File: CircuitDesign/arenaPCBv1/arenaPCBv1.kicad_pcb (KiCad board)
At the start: 2 copper layers, 13 parts, among them Q1 IRF520N

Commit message: PCB v1 finished
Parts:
- removed D2: LED, LED_THT:LED_D3.0mm
- removed U2: ~, Connector_PinHeader_1.27mm:PinHeader_1x03_P1.27mm_Vertical
- added C2: 100uF, Capacitor_THT:CP_Radial_D8.0mm_P3.50mm, F.Cu at (121.9, 104.2)
- added C3: 10uF, Capacitor_THT:CP_Radial_D5.0mm_P2.00mm, F.Cu at (152.3, 94.1)
- added C4: 100nF, Capacitor_THT:C_Disc_D3.8mm_W2.6mm_P2.50mm, F.Cu at (152.3, 76.2)
- added C5: 100nF, Capacitor_THT:C_Disc_D3.8mm_W2.6mm_P2.50mm, F.Cu at (152.3, 80.3)
- added C6: 10uF, Capacitor_THT:CP_Radial_D5.0mm_P2.00mm, F.Cu at (152.3, 100.7)
- added J1: ~, Connector_TE-Connectivity:TE_826576-2_1x02_P3.96mm_Vertical, F.Cu at (131.1, 103.6)
- added J2: ~, Connector_JST:JST_PH_B4B-PH-K_1x04_P2.00mm_Vertical, F.Cu at (109.7, 86.5)
- added J3: ~, Connector_JST:JST_PH_B2B-PH-K_1x02_P2.00mm_Vertical, F.Cu at (152.9, 106.7)
- added J4: ~, Connector_JST:JST_PH_B4B-PH-K_1x04_P2.00mm_Vertical, F.Cu at (109.7, 93.1)
- added J5: ~, Connector_PinSocket_2.00mm:PinSocket_1x02_P2.00mm_Vertical, F.Cu at (135.2, 93.6)
- added R2: 4k7, Resistor_THT:R_Axial_DIN0207_L6.3mm_D2.5mm_P15.24mm_Horizontal, F.Cu at (141.9, 68.0)
- added R3: 4k7, Resistor_THT:R_Axial_DIN0207_L6.3mm_D2.5mm_P15.24mm_Horizontal, F.Cu at (141.9, 72.1)
- C1: value C -> 220uF; footprint Capacitor_THT:CP_Radial_D13.0mm_P2.50mm -> Capacitor_THT:CP_Radial_D10.0mm_P5.00mm
- D1: value D -> 1N400X
- R1: value R -> 1k1; footprint Resistor_THT:R_Axial_DIN0207_L6.3mm_D2.5mm_P10.16mm_Horizontal -> Resistor_THT:R_Axial_DIN0207_L6.3mm_D2.5mm_P15.24mm_Horizontal
- U3: footprint Connector:JWT_A3963_1x02_P3.96mm_Vertical -> TerminalBlock_Phoenix:TerminalBlock_Phoenix_PT-1,5-2-3.5-H_1x02_P3.50mm_Horizontal
- U5: footprint Connector_PinHeader_1.27mm:PinHeader_1x06_P1.27mm_Vertical -> Connector_JST:JST_XH_B6B-XH-A_1x06_P2.50mm_Vertical
- U6: footprint 1_Bachelors_Footprints:2x7_test -> Connector_JST:JST_PHD_B16B-PHDSS_2x08_P2.00mm_Vertical
- U7: footprint Connector_PinHeader_1.27mm:PinHeader_1x04_P1.27mm_Vertical -> Connector_JST:JST_XH_B4B-XH-A_1x04_P2.50mm_Vertical
- moved U7 44.3 mm to (122.2, 95.0)
- moved D1 44.2 mm to (108.3, 108.3)
- moved R1 43.1 mm to (141.9, 64.0)
- moved U3 38.8 mm to (109.5, 101.0)
- moved U5 19.6 mm to (122.2, 87.2)
- moved Q1 18.4 mm to (141.4, 106.3)
- moved C1 17.4 mm to (141.7, 96.6)
- moved F1 14.8 mm to (143.0, 75.8)
- moved U1 11.9 mm to (108.8, 64.0)
- moved U4 11.9 mm to (125.6, 64.0)
- moved U6 11.1 mm to (141.6, 86.3)
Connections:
- C1 pad 1: S -> +12V
- C1 pad 2: D -> GND
- D1 pad 1: S -> +12V
- D1 pad 2: D -> GND
- F1 pad 2: S -> +12V
- Q1 pad 1: G -> /G
- Q1 pad 2: D -> /D
- Q1 pad 3: S -> +12V
- R1 pad 1: S -> +12V
- U1 pad 1: D -> GND
- U1 pad 15: S -> GND
- U1 pad 16: S -> +12V
- U1 pad 5: VMCU -> +3.3V
- U1 pad 6: VMCU -> +3.3V
- U1 pad 9: GND_MCU -> GND
- U3 pad 2: D -> GND
- U4 pad 1: D -> GND
- U4 pad 13: VMCU -> +3.3V
- U4 pad 2: VMCU -> +3.3V
- U4 pad 7: S -> +12V
- U4 pad 8: D -> GND
- U4 pad 9: D -> GND
- U5 pad 2: D -> GND
- U5 pad 3: Net-(U5-RST) -> Net-(U5-Pin_3)
- U5 pad 4: Net-(U5-GPIO0) -> Net-(U5-Pin_4)
- U5 pad 5: VMCU -> +3.3V
- U6 pad 1: VMCU -> GND
- U6 pad 10: Net-(U4-AIN2) -> Net-(U4-AIN1)
- U6 pad 11: Net-(U5-GPIO0) -> Net-(U5-Pin_3)
- U6 pad 12: Net-(U5-RST) -> Net-(U5-Pin_4)
- U6 pad 13: Net-(U2-SIGNAL) -> /G
- U6 pad 14: G -> Net-(J3-COM)
- U6 pad 2: GND_MCU -> +3.3V
- U6 pad 3: Net-(U1-STEP) -> Net-(U1-DIR)
- U6 pad 4: Net-(U1-DIR) -> Net-(U1-STEP)
- U6 pad 5: Net-(U1-MS3) -> Net-(U1-MS2)
- U6 pad 6: Net-(U1-MS2) -> Net-(U1-MS3)
- U6 pad 7: Net-(U1-MS1) -> Net-(U4-PWMA)
- U6 pad 8: Net-(U4-PWMA) -> Net-(U1-MS1)
- U6 pad 9: Net-(U4-AIN1) -> Net-(U4-AIN2)

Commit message: Before redoing PCB
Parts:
- removed U3: ~, TerminalBlock_Phoenix:TerminalBlock_Phoenix_PT-1,5-2-3.5-H_1x02_P3.50mm_Horizontal
- removed U4: ~, Module:Pololu_Breakout-16_15.2x20.3mm
- removed U5: ~, Connector_JST:JST_XH_B6B-XH-A_1x06_P2.50mm_Vertical
- removed U6: ~, Connector_JST:JST_PHD_B16B-PHDSS_2x08_P2.00mm_Vertical
- removed U7: ~, Connector_JST:JST_XH_B4B-XH-A_1x04_P2.50mm_Vertical
- added D2: STTH15RQ06, Package_TO_SOT_SMD:TO-263-2, F.Cu at (218.6, 61.2)
- added J6: ~, 2_Bachelors_footprints:LP127, F.Cu at (127.0, 99.1)
- added J7: ~, 2_Bachelors_footprints:CONN_B4P-VH_JST, F.Cu at (195.6, 61.0)
- added J8: ~, 2_Bachelors_footprints:CONN_B6B_VH_JST, F.Cu at (196.4, 87.1)
- added J9: ~, Connector_JST:JST_PHD_B16B-PHDSS_2x08_P2.00mm_Vertical, F.Cu at (149.9, 69.0)
- added R4: 330R, Resistor_SMD:R_1210_3225Metric_Pad1.30x2.65mm_HandSolder, F.Cu at (210.8, 69.5)
- added U2: ~, Module:Pololu_Breakout-16_15.2x20.3mm, F.Cu at (167.6, 90.2)
- C2: footprint Capacitor_THT:CP_Radial_D8.0mm_P3.50mm -> Capacitor_SMD:CP_Elec_10x10.5
- C3, C6: footprint Capacitor_THT:CP_Radial_D5.0mm_P2.00mm -> Capacitor_SMD:CP_Elec_6.3x4.5
- C4, C5: footprint Capacitor_THT:C_Disc_D3.8mm_W2.6mm_P2.50mm -> Capacitor_SMD:C_1210_3225Metric_Pad1.33x2.70mm_HandSolder
- D1: value 1N400X -> STTH15RQ06; footprint Diode_THT:D_DO-35_SOD27_P7.62mm_Horizontal -> Package_TO_SOT_SMD:TO-263-2
- F1: value RXEF300 -> MF-RG650-0; footprint Fuse:Fuse_Bourns_MF-RHT300 -> Fuse:Fuse_Bourns_MF-RG650
- J1: footprint Connector_TE-Connectivity:TE_826576-2_1x02_P3.96mm_Vertical -> 2_Bachelors_footprints:conn2_1-1123723-2_TEC
- J2, J4: footprint Connector_JST:JST_PH_B4B-PH-K_1x04_P2.00mm_Vertical -> 2_Bachelors_footprints:CONN_B4B-ZRLFSN_JST
- J3: footprint Connector_JST:JST_PH_B2B-PH-K_1x02_P2.00mm_Vertical -> 2_Bachelors_footprints:CONN_B2B-ZRLFSN_JST
- J5: footprint Connector_PinSocket_2.00mm:PinSocket_1x02_P2.00mm_Vertical -> Connector_PinSocket_2.54mm:PinSocket_1x02_P2.54mm_Vertical
- Q1: value IRF520N -> IRLB3034; footprint Package_TO_SOT_THT:TO-220-3_Vertical -> 2_Bachelors_footprints:IRF520N
- R1: value 1k1 -> 3K3; footprint Resistor_THT:R_Axial_DIN0207_L6.3mm_D2.5mm_P15.24mm_Horizontal -> Resistor_SMD:R_2512_6332Metric_Pad1.40x3.35mm_HandSolder
- R2, R3: value 4k7 -> 2K2; footprint Resistor_THT:R_Axial_DIN0207_L6.3mm_D2.5mm_P15.24mm_Horizontal -> Resistor_SMD:R_1210_3225Metric_Pad1.30x2.65mm_HandSolder
- moved C2 68.2 mm to (168.0, 53.8)
- moved U1 59.4 mm to (167.6, 72.4), turned to 90 degrees
- moved J3 52.1 mm to (160.0, 55.1), turned to -90 degrees
- moved C4 39.8 mm to (182.9, 101.6)
- moved D1 33.9 mm to (141.0, 99.1)
- moved J4 33.5 mm to (127.3, 64.5)
- moved J2 33.1 mm to (127.3, 58.4)
- moved C3 31.2 mm to (183.4, 96.5)
- moved J1 29.2 mm to (160.0, 99.1)
- moved C5 27.8 mm to (170.1, 101.6), turned to 180 degrees
- moved Q1 23.7 mm to (157.5, 88.9), turned to 180 degrees
- moved C6 18.3 mm to (170.2, 96.5), turned to 180 degrees
- moved R1 17.4 mm to (129.5, 76.2), turned to -90 degrees
- moved F1 17.2 mm to (135.9, 91.4), turned to 90 degrees
- moved C1 10.2 mm to (142.3, 86.4)
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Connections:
- D1 pad 1: +12V -> (no net)
- D1 pad 2: GND -> +12V
- J1 pad 1: /D -> +12V
- J1 pad 2: GND -> /D
- J2 pad 2: /SDA -> /SCL
- J2 pad 3: /SCL -> /SDA
- J4 pad 2: /SDA -> /SCL
- J4 pad 3: /SCL -> /SDA
- Q1 pad 3: +12V -> GND
- R2 pad 2: /SDA -> /SCL
- R3 pad 2: /SCL -> /SDA
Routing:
- net (no net): track 0.00 -> 404.0 mm, vias 0 -> 1
- net GND: track 0.00 -> 310.4 mm
- net +12V: track 0.00 -> 156.9 mm, vias 0 -> 1
- net +3.3V: track 0.00 -> 136.6 mm, vias 0 -> 1
- net /G: track 0.00 -> 39.5 mm
- net /SCL: track 0.00 -> 35.1 mm
- net Net-(J8-Pin_6): track 0.00 -> 31.3 mm
- net /SDA: track 0.00 -> 30.7 mm
- net Net-(J8-Pin_1): track 0.00 -> 28.2 mm
- net Net-(J7-Pin_1): track 0.00 -> 26.8 mm
- net Net-(J7-Pin_2): track 0.00 -> 25.2 mm
- net Net-(J7-Pin_3): track 0.00 -> 23.4 mm
- net Net-(J7-Pin_4): track 0.00 -> 21.7 mm
- net /D: track 0.00 -> 10.4 mm
- net Net-(J3-COM): track 0.00 -> 9.23 mm
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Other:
- board outline added: 96 x 69.6 mm

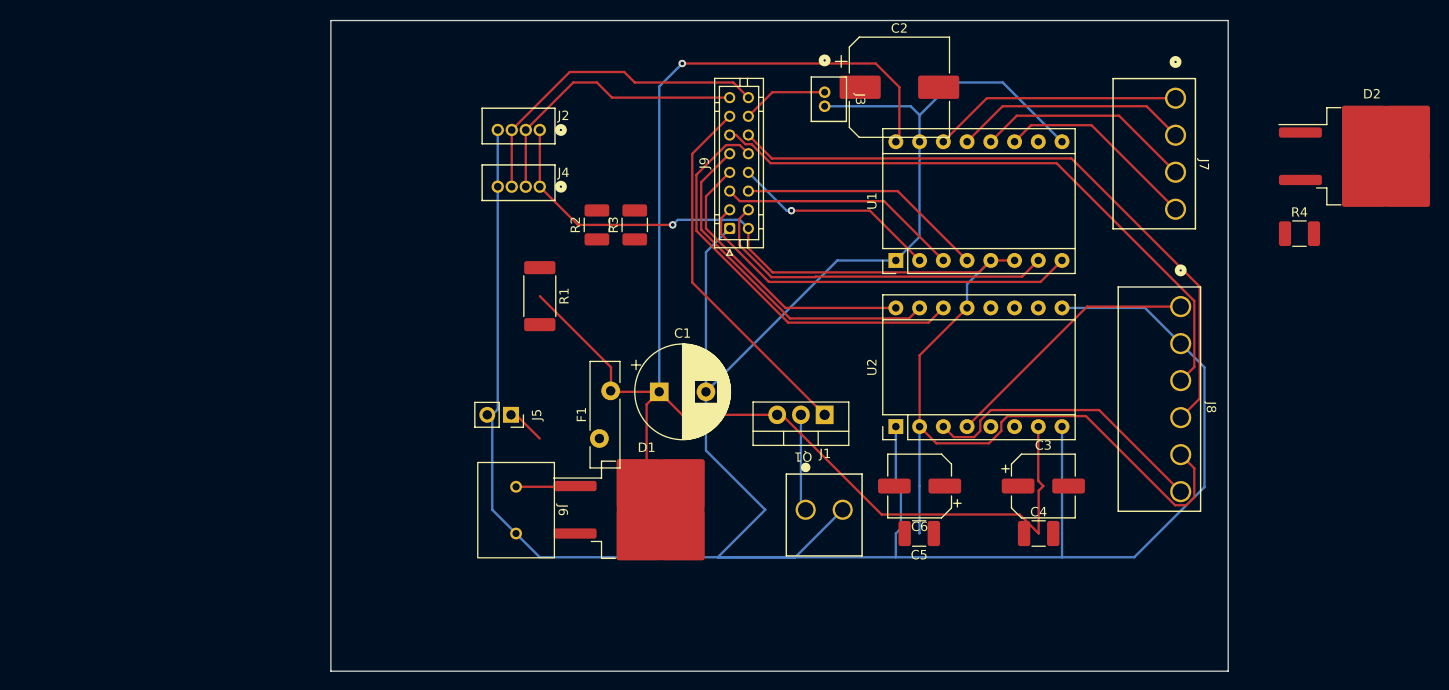
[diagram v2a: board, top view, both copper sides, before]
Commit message: PCB v2 finished, diode needs changing
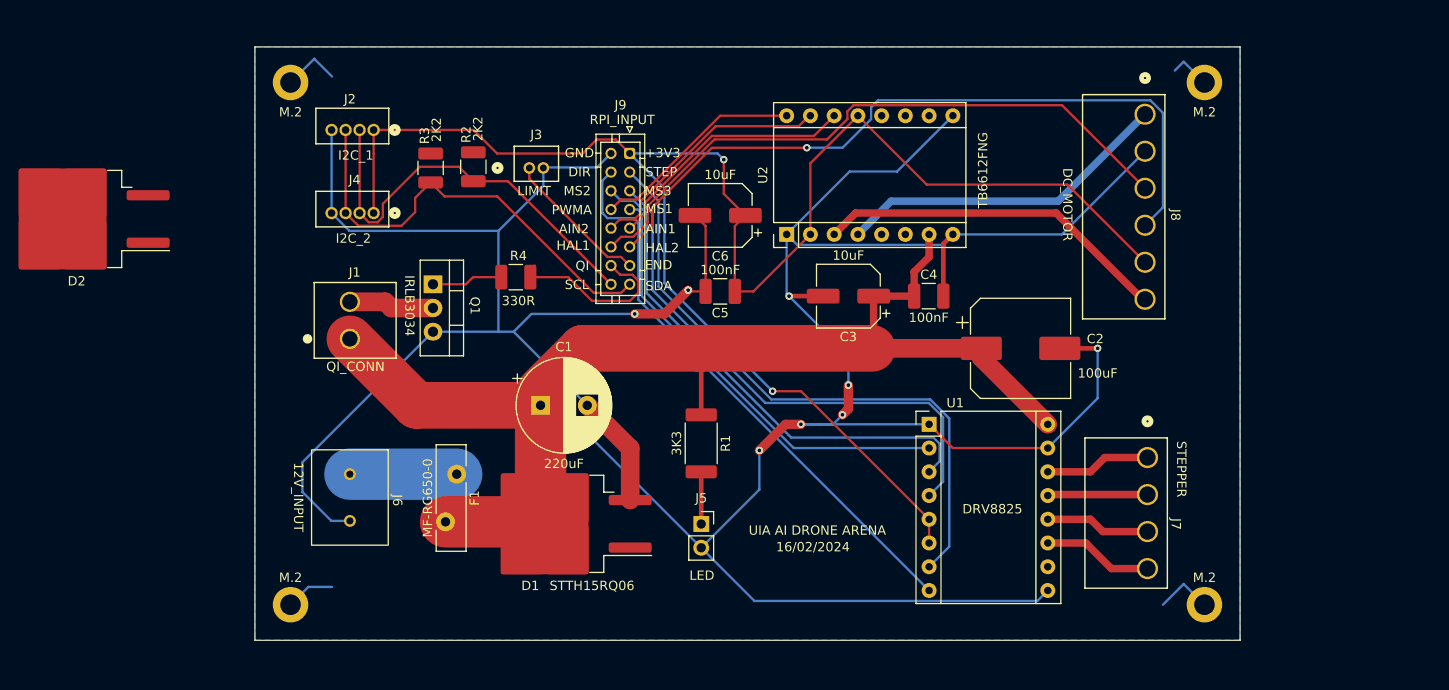
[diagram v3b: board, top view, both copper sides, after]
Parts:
- added M.2: MountingHole_2.2mm_M2_DIN965_Pad, MountingHole:MountingHole_2.2mm_M2_DIN965_Pad, F.Cu at (102.9, 53.3)
- added M.2: MountingHole_2.2mm_M2_DIN965_Pad, MountingHole:MountingHole_2.2mm_M2_DIN965_Pad, F.Cu at (200.7, 109.2)
- added M.2: MountingHole_2.2mm_M2_DIN965_Pad, MountingHole:MountingHole_2.2mm_M2_DIN965_Pad, F.Cu at (102.9, 109.2)
- added M.2: MountingHole_2.2mm_M2_DIN965_Pad, MountingHole:MountingHole_2.2mm_M2_DIN965_Pad, F.Cu at (200.7, 53.3)
- moved D2 138.8 mm to (80.0, 67.9), turned to 180 degrees
- moved R4 84.0 mm to (127.0, 74.2), turned to 180 degrees
- moved J1 54.7 mm to (109.2, 78.7), turned to 90 degrees
- moved Q1 41.0 mm to (118.1, 77.5), turned to -90 degrees
- moved J7 38.6 mm to (192.6, 99.4)
- moved C6 36.0 mm to (148.8, 67.6)
- moved C5 33.5 mm to (148.8, 75.7)
- moved J3 31.8 mm to (129.1, 62.5), turned to 0 degrees
- moved C2 30.8 mm to (181.0, 81.8)
- moved C3 29.1 mm to (162.6, 76.2), turned to 180 degrees
- moved C4 28.0 mm to (171.2, 76.2)
- moved U2 23.7 mm to (156.0, 69.6)
- moved J5 23.5 mm to (146.8, 100.6), turned to 0 degrees
- moved R1 23.4 mm to (146.8, 92.0)
- moved R3 22.7 mm to (117.9, 62.5), turned to -90 degrees
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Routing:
- net (no net): track 404.0 -> 0.00 mm, vias 1 -> 0
- net GND: track 310.4 -> 396.4 mm, vias 0 -> 8
- net Net-(J8-Pin_4): track 0.00 -> 78.8 mm, vias 0 -> 1
- net Net-(J8-Pin_3): track 0.00 -> 68.6 mm
- net Net-(J9-STEP): track 0.00 -> 67.2 mm
- net Net-(J9-DIR): track 0.00 -> 61.3 mm
- net Net-(J9-MS3): track 0.00 -> 57.4 mm
- net Net-(J9-MS2): track 0.00 -> 54.8 mm
- net Net-(J9-MS1): track 0.00 -> 47.8 mm
- net +3.3V: track 136.6 -> 183.8 mm, vias 1 -> 2
- net /G: track 39.5 -> 7.63 mm
- net Net-(J9-AIN1): track 0.00 -> 27.5 mm
- net Net-(J9-AIN2): track 0.00 -> 27.1 mm
- net +12V: track 156.9 -> 130.0 mm, vias 1 -> 0
- net Net-(J9-PWMA): track 0.00 -> 23.0 mm
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- added copper zone on B.Cu, net GND
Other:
- board size 96 x 69.6 mm -> 105.4 x 63.5 mm
- board text added: "+3V3"
- board text added: "12V_INPUT"
- board text added: "16/02/2024"
- board text added: "AIN1"
- board text added: "AIN2"
- board text added: "DC_MOTOR"
- board text added: "DIR"
- board text added: "DRV8825"
- board text added: "END"
- board text added: "GND"
- board text added: "HAL1"
- board text added: "HAL2"
- board text added: "I2C_1"
- board text added: "I2C_2"
- board text added: "LED"
- board text added: "LIMIT"
- board text added: "MS1"
- board text added: "MS2"
- board text added: "MS3"
- board text added: "PWMA"
- board text added: "QI"
- board text added: "QI_CONN"
- board text added: "RPI_INPUT"
- board text added: "SCL"
- board text added: "SDA"
- board text added: "STEP"
- board text added: "STEPPER"
- board text added: "TB6612FNG"
- board text added: "UIA AI DRONE ARENA"

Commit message: PCB before adding thermal relief
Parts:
- removed D2: STTH15RQ06, Package_TO_SOT_SMD:TO-263-2
- moved C3 3.24 mm to (165.7, 75.6)
- moved C4 2.91 mm to (173.4, 74.3)
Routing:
- net GND: track 396.4 -> 395.2 mm
- added copper zone on F.Cu, net +12V

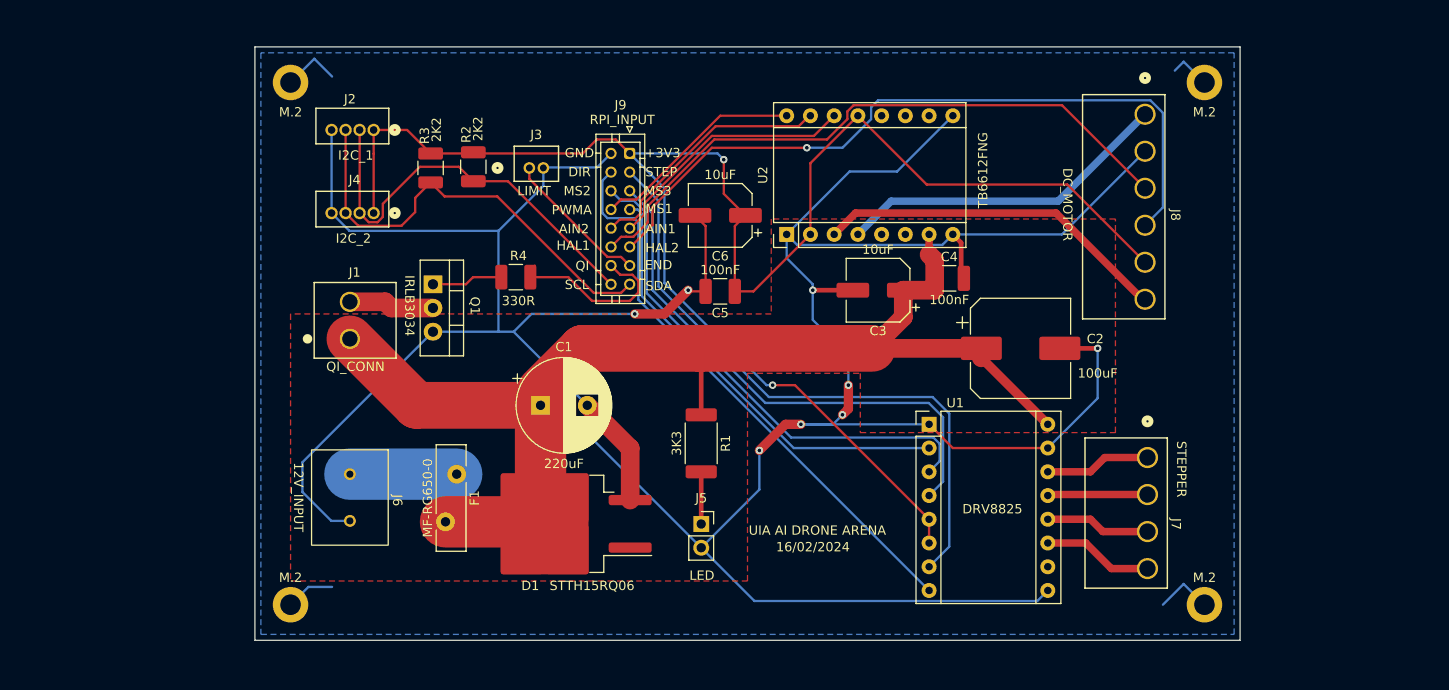
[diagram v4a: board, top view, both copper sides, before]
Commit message: pcb done before changing diodes and C1
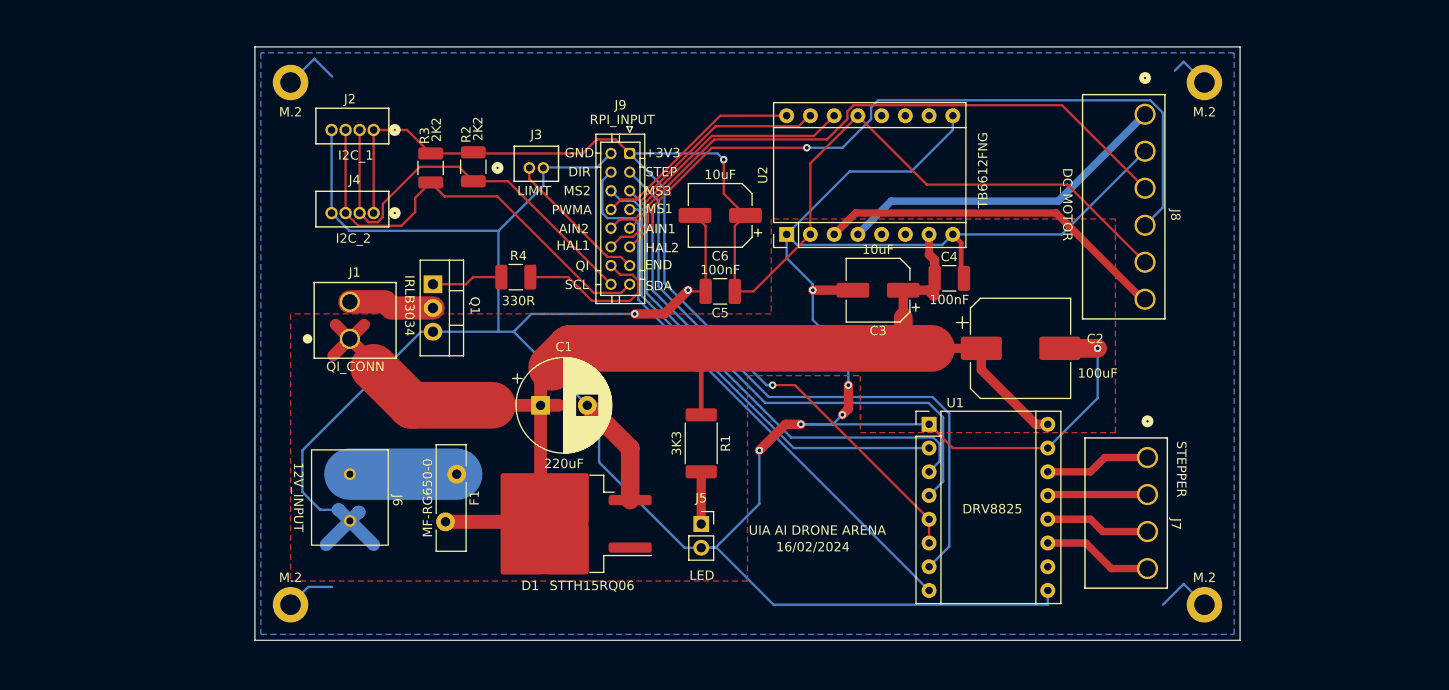
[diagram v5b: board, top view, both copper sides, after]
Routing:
- net +12V: track 129.9 -> 144.2 mm
- net GND: track 395.2 -> 408.6 mm
